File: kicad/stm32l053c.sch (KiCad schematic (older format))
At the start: 17 parts, among them P1 SWD, U1 STM32L053C8_LQFP48, U2 TLV61225, Y1 Crystal

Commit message: Buttons
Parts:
- added SW1, SW2, SW3: SW_PUSH, symbol SW_PUSH
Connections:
- net BUTTON0: now also SW1.2
- net BUTTON1: now also SW2.2
- net BUTTON2: now also SW3.2
- net VDD: now also SW1.1, SW2.1, SW3.1
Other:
- moved on the sheet: P1
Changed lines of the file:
@@
 $EndDescr
 $Comp
-L Earth #PWR4
+L Earth #PWR21
 U 1 1 58021BE1
 P 4900 7200
-F 0 "#PWR4" H 4900 6950 50  0001 C CNN
+F 0 "#PWR21" H 4900 6950 50  0001 C CNN
 F 1 "Earth" H 4900 7050 50  0001 C CNN
 F 2 "" H 4900 7200 50  0000 C CNN
@@
 $EndComp
 $Comp
-L VDD #PWR2
+L VDD #PWR19
 U 1 1 58021C2A
 P 4900 6900
-F 0 "#PWR2" H 4900 6750 50  0001 C CNN
+F 0 "#PWR19" H 4900 6750 50  0001 C CNN
 F 1 "VDD" H 4900 7050 50  0000 C CNN
 F 2 "" H 4900 6900 50  0000 C CNN
@@
 $EndComp
 $Comp
-L GNDA #PWR20
+L GNDA #PWR13
 U 1 1 58021F75
 P 5100 6300
-F 0 "#PWR20" H 5100 6050 50  0001 C CNN
+F 0 "#PWR13" H 5100 6050 50  0001 C CNN
 F 1 "GNDA" H 5100 6150 50  0000 C CNN
 F 2 "" H 5100 6300 50  0000 C CNN
@@
 $EndComp
 $Comp
-L Earth #PWR21
+L Earth #PWR14
 U 1 1 58021F89
 P 5600 6300
-F 0 "#PWR21" H 5600 6050 50  0001 C CNN
+F 0 "#PWR14" H 5600 6050 50  0001 C CNN
 F 1 "Earth" H 5600 6150 50  0001 C CNN
 F 2 "" H 5600 6300 50  0000 C CNN
@@
 $EndComp
 $Comp
-L GNDA #PWR18
+L GNDA #PWR11
 U 1 1 58022154
 P 5150 5800
-F 0 "#PWR18" H 5150 5550 50  0001 C CNN
+F 0 "#PWR11" H 5150 5550 50  0001 C CNN
 F 1 "GNDA" H 5150 5650 50  0000 C CNN
 F 2 "" H 5150 5800 50  0000 C CNN
@@
 $EndComp
 $Comp
-L Earth #PWR19
+L Earth #PWR12
 U 1 1 580221FA
 P 5650 5800
-F 0 "#PWR19" H 5650 5550 50  0001 C CNN
+F 0 "#PWR12" H 5650 5550 50  0001 C CNN
 F 1 "Earth" H 5650 5650 50  0001 C CNN
 F 2 "" H 5650 5800 50  0000 C CNN
@@
 $EndComp
 $Comp
-L Earth #PWR7
+L Earth #PWR4
 U 1 1 5803310F
 P 4800 1800
-F 0 "#PWR7" H 4800 1550 50  0001 C CNN
+F 0 "#PWR4" H 4800 1550 50  0001 C CNN
 F 1 "Earth" H 4800 1650 50  0001 C CNN
 F 2 "" H 4800 1800 50  0000 C CNN
@@
 L CONN_01X05 P1
 U 1 1 58036840
-P 1700 3550
-F 0 "P1" H 1700 3900 50  0000 C CNN
-F 1 "SWD" V 1800 3550 50  0000 C CNN
-F 2 "Pin_Headers:Pin_Header_Straight_1x06" H 1700 3550 50  0001 C CNN
-F 3 "" H 1700 3550 50  0000 C CNN
-	1    1700 3550
+P 1450 1400
+F 0 "P1" H 1450 1750 50  0000 C CNN
+F 1 "SWD" V 1550 1400 50  0000 C CNN
+F 2 "Pin_Headers:Pin_Header_Straight_1x06" H 1450 1400 50  0001 C CNN
+F 3 "" H 1450 1400 50  0000 C CNN
+	1    1450 1400
 	-1   0    0    -1
 $EndComp
 $Comp
-L Earth #PWR6
+L Earth #PWR3
 U 1 1 580369A9
-P 2400 3550
-F 0 "#PWR6" H 2400 3300 50  0001 C CNN
-F 1 "Earth" H 2400 3400 50  0001 C CNN
-F 2 "" H 2400 3550 50  0000 C CNN
-F 3 "" H 2400 3550 50  0000 C CNN
-	1    2400 3550
-	1    0    0    -1
-$EndComp
-Text GLabel 1900 3450 2    60   Input ~ 0
+P 2150 1400
+F 0 "#PWR3" H 2150 1150 50  0001 C CNN
+F 1 "Earth" H 2150 1250 50  0001 C CNN
+F 2 "" H 2150 1400 50  0000 C CNN
+F 3 "" H 2150 1400 50  0000 C CNN
+	1    2150 1400
+	1    0    0    -1
+$EndComp
+Text GLabel 1650 1300 2    60   Input ~ 0
 SWCLK
-Text GLabel 1900 3650 2    60   Input ~ 0
+Text GLabel 1650 1500 2    60   Input ~ 0
 SWDIO
-Text GLabel 1900 3750 2    60   Input ~ 0
+Text GLabel 1650 1600 2    60   Input ~ 0
 NRST
 $Comp
-L VDD #PWR3
+L VDD #PWR2
 U 1 1 5803734F
-P 1900 3350
-F 0 "#PWR3" H 1900 3200 50  0001 C CNN
-F 1 "VDD" H 1900 3500 50  0000 C CNN
-F 2 "" H 1900 3350 50  0000 C CNN
-F 3 "" H 1900 3350 50  0000 C CNN
-	1    1900 3350
+P 1650 1200
+F 0 "#PWR2" H 1650 1050 50  0001 C CNN
+F 1 "VDD" H 1650 1350 50  0000 C CNN
+F 2 "" H 1650 1200 50  0000 C CNN
+F 3 "" H 1650 1200 50  0000 C CNN
+	1    1650 1200
 	1    0    0    -1
 $EndComp
@@
 $EndComp
 $Comp
-L Earth #PWR5
+L Earth #PWR22
 U 1 1 5803BDC8
 P 5950 7200
-F 0 "#PWR5" H 5950 6950 50  0001 C CNN
+F 0 "#PWR22" H 5950 6950 50  0001 C CNN
 F 1 "Earth" H 5950 7050 50  0001 C CNN
 F 2 "" H 5950 7200 50  0000 C CNN
@@
 $EndComp
 $Comp
-L Earth #PWR16
+L Earth #PWR9
 U 1 1 58065816
 P 6550 5400
-F 0 "#PWR16" H 6550 5150 50  0001 C CNN
+F 0 "#PWR9" H 6550 5150 50  0001 C CNN
 F 1 "Earth" H 6550 5250 50  0001 C CNN
 F 2 "" H 6550 5400 50  0000 C CNN
@@
 	4050 3700 4600 3700
 Wire Wire Line
-	2400 3550 1900 3550
+	2150 1400 1650 1400
 Wire Wire Line
 	5600 6300 5100 6300
@@
 $EndComp
 $Comp
-L Earth #PWR17
+L Earth #PWR10
 U 1 1 5806680D
 P 3600 5700
-F 0 "#PWR17" H 3600 5450 50  0001 C CNN
+F 0 "#PWR10" H 3600 5450 50  0001 C CNN
 F 1 "Earth" H 3600 5550 50  0001 C CNN
 F 2 "" H 3600 5700 50  0000 C CNN
@@
 $EndComp
 $Comp
-L Earth #PWR15
+L Earth #PWR5
 U 1 1 58077163
 P 9600 2300
-F 0 "#PWR15" H 9600 2050 50  0001 C CNN
+F 0 "#PWR5" H 9600 2050 50  0001 C CNN
 F 1 "Earth" H 9600 2150 50  0001 C CNN
 F 2 "" H 9600 2300 50  0000 C CNN
@@
 $EndComp
 $Comp
-L +BATT #PWR10
+L +BATT #PWR16
 U 1 1 584F2368
 P 850 6750
-F 0 "#PWR10" H 850 6600 50  0001 C CNN
+F 0 "#PWR16" H 850 6600 50  0001 C CNN
 F 1 "+BATT" H 850 6890 50  0000 C CNN
 F 2 "" H 850 6750 50  0000 C CNN
@@
 Connection ~ 2700 6550
 $Comp
-L Earth #PWR13
+L Earth #PWR18
 U 1 1 584F287E
 P 2850 6850
-F 0 "#PWR13" H 2850 6600 50  0001 C CNN
+F 0 "#PWR18" H 2850 6600 50  0001 C CNN
 F 1 "Earth" H 2850 6700 50  0001 C CNN
 F 2 "" H 2850 6850 50  0000 C CNN
@@
 $EndComp
 $Comp
-L Earth #PWR12
+L Earth #PWR17
 U 1 1 584F28E3
 P 1700 6850
-F 0 "#PWR12" H 1700 6600 50  0001 C CNN
+F 0 "#PWR17" H 1700 6600 50  0001 C CNN
 F 1 "Earth" H 1700 6700 50  0001 C CNN
 F 2 "" H 1700 6850 50  0000 C CNN
@@
 $EndComp
 $Comp
-L Earth #PWR14
+L Earth #PWR20
 U 1 1 584F2924
 P 1250 7050
-F 0 "#PWR14" H 1250 6800 50  0001 C CNN
+F 0 "#PWR20" H 1250 6800 50  0001 C CNN
 F 1 "Earth" H 1250 6900 50  0001 C CNN
 F 2 "" H 1250 7050 50  0000 C CNN
@@
 $EndComp
 $Comp
-L VDD #PWR9
+L VDD #PWR15
 U 1 1 584F2A51
 P 3200 6550
-F 0 "#PWR9" H 3200 6400 50  0001 C CNN
+F 0 "#PWR15" H 3200 6400 50  0001 C CNN
 F 1 "VDD" H 3200 6700 50  0000 C CNN
 F 2 "" H 3200 6550 50  0000 C CNN
@@
 Wire Wire Line
 	8500 4550 9050 4550
+$Comp
+L SW_PUSH SW1
+U 1 1 5850680E
+P 1700 2900
+F 0 "SW1" H 1850 3010 50  0000 C CNN
+F 1 "SW_PUSH" H 1700 2820 50  0000 C CNN
+F 2 "" H 1700 2900 50  0000 C CNN
+F 3 "" H 1700 2900 50  0000 C CNN
+	1    1700 2900
+	1    0    0    -1
+$EndComp
+$Comp
+L VDD #PWR6
+U 1 1 585069C3
+P 1300 2750
+F 0 "#PWR6" H 1300 2600 50  0001 C CNN
+F 1 "VDD" H 1300 2900 50  0000 C CNN
+F 2 "" H 1300 2750 50  0000 C CNN
+F 3 "" H 1300 2750 50  0000 C CNN
+	1    1300 2750
+	1    0    0    -1
+$EndComp
+Text Label 2550 2900 2    60   ~ 0
+BUTTON0
+Wire Wire Line
+	1300 2750 1300 2900
+Wire Wire Line
+	1300 2900 1400 2900
+Wire Wire Line
+	2000 2900 2550 2900
+$Comp
+L SW_PUSH SW2
+U 1 1 58506BDE
+P 1700 3450
+F 0 "SW2" H 1850 3560 50  0000 C CNN
+F 1 "SW_PUSH" H 1700 3370 50  0000 C CNN
+F 2 "" H 1700 3450 50  0000 C CNN
+F 3 "" H 1700 3450 50  0000 C CNN
+	1    1700 3450
+	1    0    0    -1
+$EndComp
+$Comp
+L VDD #PWR7
+U 1 1 58506BE4
+P 1300 3300
+F 0 "#PWR7" H 1300 3150 50  0001 C CNN
+F 1 "VDD" H 1300 3450 50  0000 C CNN
+F 2 "" H 1300 3300 50  0000 C CNN
+F 3 "" H 1300 3300 50  0000 C CNN
+	1    1300 3300
+	1    0    0    -1
+$EndComp
+Text Label 2550 3450 2    60   ~ 0
+BUTTON1
+Wire Wire Line
+	1300 3300 1300 3450
+Wire Wire Line
+	1300 3450 1400 3450
+Wire Wire Line
+	2000 3450 2550 3450
+$Comp
+L SW_PUSH SW3
+U 1 1 58506C80
+P 1700 4050
+F 0 "SW3" H 1850 4160 50  0000 C CNN
+F 1 "SW_PUSH" H 1700 3970 50  0000 C CNN
+F 2 "" H 1700 4050 50  0000 C CNN
+F 3 "" H 1700 4050 50  0000 C CNN
+	1    1700 4050
+	1    0    0    -1
+$EndComp
+$Comp
+L VDD #PWR8
+U 1 1 58506C86
+P 1300 3900
+F 0 "#PWR8" H 1300 3750 50  0001 C CNN
+F 1 "VDD" H 1300 4050 50  0000 C CNN
+F 2 "" H 1300 3900 50  0000 C CNN
+F 3 "" H 1300 3900 50  0000 C CNN
+	1    1300 3900
+	1    0    0    -1
+$EndComp
+Text Label 2550 4050 2    60   ~ 0
+BUTTON2
+Wire Wire Line
+	1300 3900 1300 4050
+Wire Wire Line
+	1300 4050 1400 4050
+Wire Wire Line
+	2000 4050 2550 4050
 $EndSCHEMATC

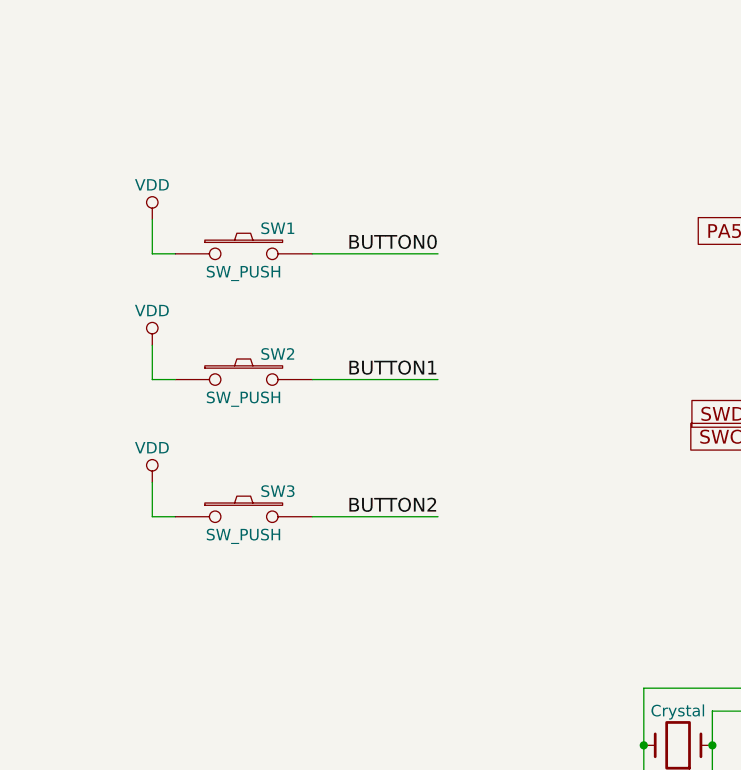
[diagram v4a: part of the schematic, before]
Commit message: Button debounce
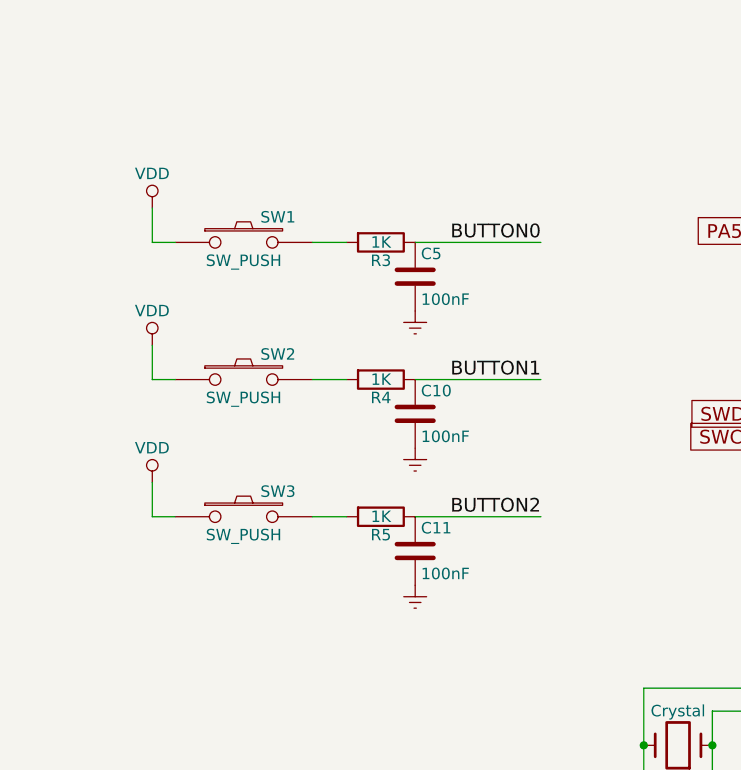
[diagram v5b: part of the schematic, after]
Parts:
- added C10, C11, C5: 100nF, symbol C
- added R3, R4, R5: 1K, symbol R
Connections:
- net BUTTON0: now also C5.1, R3.1; no longer SW1.2
- net BUTTON1: now also C10.1, R4.1; no longer SW2.2
- net BUTTON2: now also C11.1, R5.1; no longer SW3.2
- net Earth: now also C10.2, C11.2, C5.2
- new net: R3.2, SW1.2
- new net: R4.2, SW2.2
- new net: R5.2, SW3.2
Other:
- moved on the sheet: SW1
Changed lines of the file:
@@
 $EndDescr
 $Comp
-L Earth #PWR21
+L Earth #PWR24
 U 1 1 58021BE1
 P 4900 7200
-F 0 "#PWR21" H 4900 6950 50  0001 C CNN
+F 0 "#PWR24" H 4900 6950 50  0001 C CNN
 F 1 "Earth" H 4900 7050 50  0001 C CNN
 F 2 "" H 4900 7200 50  0000 C CNN
@@
 $EndComp
 $Comp
-L VDD #PWR19
+L VDD #PWR22
 U 1 1 58021C2A
 P 4900 6900
-F 0 "#PWR19" H 4900 6750 50  0001 C CNN
+F 0 "#PWR22" H 4900 6750 50  0001 C CNN
 F 1 "VDD" H 4900 7050 50  0000 C CNN
 F 2 "" H 4900 6900 50  0000 C CNN
@@
 $EndComp
 $Comp
-L GNDA #PWR13
+L GNDA #PWR16
 U 1 1 58021F75
 P 5100 6300
-F 0 "#PWR13" H 5100 6050 50  0001 C CNN
+F 0 "#PWR16" H 5100 6050 50  0001 C CNN
 F 1 "GNDA" H 5100 6150 50  0000 C CNN
 F 2 "" H 5100 6300 50  0000 C CNN
@@
 $EndComp
 $Comp
-L Earth #PWR14
+L Earth #PWR17
 U 1 1 58021F89
 P 5600 6300
-F 0 "#PWR14" H 5600 6050 50  0001 C CNN
+F 0 "#PWR17" H 5600 6050 50  0001 C CNN
 F 1 "Earth" H 5600 6150 50  0001 C CNN
 F 2 "" H 5600 6300 50  0000 C CNN
@@
 $EndComp
 $Comp
-L GNDA #PWR11
+L GNDA #PWR14
 U 1 1 58022154
 P 5150 5800
-F 0 "#PWR11" H 5150 5550 50  0001 C CNN
+F 0 "#PWR14" H 5150 5550 50  0001 C CNN
 F 1 "GNDA" H 5150 5650 50  0000 C CNN
 F 2 "" H 5150 5800 50  0000 C CNN
@@
 $EndComp
 $Comp
-L Earth #PWR12
+L Earth #PWR15
 U 1 1 580221FA
 P 5650 5800
-F 0 "#PWR12" H 5650 5550 50  0001 C CNN
+F 0 "#PWR15" H 5650 5550 50  0001 C CNN
 F 1 "Earth" H 5650 5650 50  0001 C CNN
 F 2 "" H 5650 5800 50  0000 C CNN
@@
 $EndComp
 $Comp
-L Earth #PWR22
+L Earth #PWR25
 U 1 1 5803BDC8
 P 5950 7200
-F 0 "#PWR22" H 5950 6950 50  0001 C CNN
+F 0 "#PWR25" H 5950 6950 50  0001 C CNN
 F 1 "Earth" H 5950 7050 50  0001 C CNN
 F 2 "" H 5950 7200 50  0000 C CNN
@@
 $EndComp
 $Comp
-L Earth #PWR9
+L Earth #PWR12
 U 1 1 58065816
 P 6550 5400
-F 0 "#PWR9" H 6550 5150 50  0001 C CNN
+F 0 "#PWR12" H 6550 5150 50  0001 C CNN
 F 1 "Earth" H 6550 5250 50  0001 C CNN
 F 2 "" H 6550 5400 50  0000 C CNN
@@
 $EndComp
 $Comp
-L Earth #PWR10
+L Earth #PWR13
 U 1 1 5806680D
 P 3600 5700
-F 0 "#PWR10" H 3600 5450 50  0001 C CNN
+F 0 "#PWR13" H 3600 5450 50  0001 C CNN
 F 1 "Earth" H 3600 5550 50  0001 C CNN
 F 2 "" H 3600 5700 50  0000 C CNN
@@
 $EndComp
 $Comp
-L +BATT #PWR16
+L +BATT #PWR19
 U 1 1 584F2368
 P 850 6750
-F 0 "#PWR16" H 850 6600 50  0001 C CNN
+F 0 "#PWR19" H 850 6600 50  0001 C CNN
 F 1 "+BATT" H 850 6890 50  0000 C CNN
 F 2 "" H 850 6750 50  0000 C CNN
@@
 Connection ~ 2700 6550
 $Comp
-L Earth #PWR18
+L Earth #PWR21
 U 1 1 584F287E
 P 2850 6850
-F 0 "#PWR18" H 2850 6600 50  0001 C CNN
+F 0 "#PWR21" H 2850 6600 50  0001 C CNN
 F 1 "Earth" H 2850 6700 50  0001 C CNN
 F 2 "" H 2850 6850 50  0000 C CNN
@@
 $EndComp
 $Comp
-L Earth #PWR17
+L Earth #PWR20
 U 1 1 584F28E3
 P 1700 6850
-F 0 "#PWR17" H 1700 6600 50  0001 C CNN
+F 0 "#PWR20" H 1700 6600 50  0001 C CNN
 F 1 "Earth" H 1700 6700 50  0001 C CNN
 F 2 "" H 1700 6850 50  0000 C CNN
@@
 $EndComp
 $Comp
-L Earth #PWR20
+L Earth #PWR23
 U 1 1 584F2924
 P 1250 7050
-F 0 "#PWR20" H 1250 6800 50  0001 C CNN
+F 0 "#PWR23" H 1250 6800 50  0001 C CNN
 F 1 "Earth" H 1250 6900 50  0001 C CNN
 F 2 "" H 1250 7050 50  0000 C CNN
@@
 $EndComp
 $Comp
-L VDD #PWR15
+L VDD #PWR18
 U 1 1 584F2A51
 P 3200 6550
-F 0 "#PWR15" H 3200 6400 50  0001 C CNN
+F 0 "#PWR18" H 3200 6400 50  0001 C CNN
 F 1 "VDD" H 3200 6700 50  0000 C CNN
 F 2 "" H 3200 6550 50  0000 C CNN
@@
 L SW_PUSH SW1
 U 1 1 5850680E
-P 1700 2900
-F 0 "SW1" H 1850 3010 50  0000 C CNN
-F 1 "SW_PUSH" H 1700 2820 50  0000 C CNN
-F 2 "" H 1700 2900 50  0000 C CNN
-F 3 "" H 1700 2900 50  0000 C CNN
-	1    1700 2900
+P 1700 2850
+F 0 "SW1" H 1850 2960 50  0000 C CNN
+F 1 "SW_PUSH" H 1700 2770 50  0000 C CNN
+F 2 "" H 1700 2850 50  0000 C CNN
+F 3 "" H 1700 2850 50  0000 C CNN
+	1    1700 2850
 	1    0    0    -1
 $EndComp
@@
 L VDD #PWR6
 U 1 1 585069C3
-P 1300 2750
-F 0 "#PWR6" H 1300 2600 50  0001 C CNN
-F 1 "VDD" H 1300 2900 50  0000 C CNN
-F 2 "" H 1300 2750 50  0000 C CNN
-F 3 "" H 1300 2750 50  0000 C CNN
-	1    1300 2750
-	1    0    0    -1
-$EndComp
-Text Label 2550 2900 2    60   ~ 0
+P 1300 2700
+F 0 "#PWR6" H 1300 2550 50  0001 C CNN
+F 1 "VDD" H 1300 2850 50  0000 C CNN
+F 2 "" H 1300 2700 50  0000 C CNN
+F 3 "" H 1300 2700 50  0000 C CNN
+	1    1300 2700
+	1    0    0    -1
+$EndComp
+Text Label 3000 2850 2    60   ~ 0
 BUTTON0
 Wire Wire Line
-	1300 2750 1300 2900
-Wire Wire Line
-	1300 2900 1400 2900
-Wire Wire Line
-	2000 2900 2550 2900
+	1300 2700 1300 2850
+Wire Wire Line
+	1300 2850 1400 2850
 $Comp
 L SW_PUSH SW2
@@
 $EndComp
 $Comp
-L VDD #PWR7
+L VDD #PWR8
 U 1 1 58506BE4
 P 1300 3300
-F 0 "#PWR7" H 1300 3150 50  0001 C CNN
+F 0 "#PWR8" H 1300 3150 50  0001 C CNN
 F 1 "VDD" H 1300 3450 50  0000 C CNN
 F 2 "" H 1300 3300 50  0000 C CNN
@@
 	1    0    0    -1
 $EndComp
-Text Label 2550 3450 2    60   ~ 0
+Text Label 3000 3450 2    60   ~ 0
 BUTTON1
 Wire Wire Line
@@
 Wire Wire Line
 	1300 3450 1400 3450
-Wire Wire Line
-	2000 3450 2550 3450
 $Comp
 L SW_PUSH SW3
@@
 $EndComp
 $Comp
-L VDD #PWR8
+L VDD #PWR10
 U 1 1 58506C86
 P 1300 3900
-F 0 "#PWR8" H 1300 3750 50  0001 C CNN
+F 0 "#PWR10" H 1300 3750 50  0001 C CNN
 F 1 "VDD" H 1300 4050 50  0000 C CNN
 F 2 "" H 1300 3900 50  0000 C CNN
@@
 	1    0    0    -1
 $EndComp
-Text Label 2550 4050 2    60   ~ 0
+Text Label 3000 4050 2    60   ~ 0
 BUTTON2
 Wire Wire Line
@@
 Wire Wire Line
 	1300 4050 1400 4050
-Wire Wire Line
-	2000 4050 2550 4050
+$Comp
+L R R3
+U 1 1 58519B61
+P 2300 2850
+F 0 "R3" V 2380 2850 50  0000 C CNN
+F 1 "1K" V 2300 2850 50  0000 C CNN
+F 2 "" V 2230 2850 50  0000 C CNN
+F 3 "" H 2300 2850 50  0000 C CNN
+	1    2300 2850
+	0    1    1    0
+$EndComp
+$Comp
+L R R4
+U 1 1 58519D14
+P 2300 3450
+F 0 "R4" V 2380 3450 50  0000 C CNN
+F 1 "1K" V 2300 3450 50  0000 C CNN
+F 2 "" V 2230 3450 50  0000 C CNN
+F 3 "" H 2300 3450 50  0000 C CNN
+	1    2300 3450
+	0    1    1    0
+$EndComp
+$Comp
+L R R5
+U 1 1 58519D86
+P 2300 4050
+F 0 "R5" V 2380 4050 50  0000 C CNN
+F 1 "1K" V 2300 4050 50  0000 C CNN
+F 2 "" V 2230 4050 50  0000 C CNN
+F 3 "" H 2300 4050 50  0000 C CNN
+	1    2300 4050
+	0    1    1    0
+$EndComp
+Wire Wire Line
+	2150 2850 2000 2850
+Wire Wire Line
+	2000 3450 2150 3450
+Wire Wire Line
+	2000 4050 2150 4050
+Wire Wire Line
+	2450 3450 3000 3450
+Wire Wire Line
+	2450 4050 3000 4050
+$Comp
+L C C5
+U 1 1 5851A24C
+P 2450 3000
+F 0 "C5" H 2475 3100 50  0000 L CNN
+F 1 "100nF" H 2475 2900 50  0000 L CNN
+F 2 "" H 2488 2850 50  0000 C CNN
+F 3 "" H 2450 3000 50  0000 C CNN
+	1    2450 3000
+	1    0    0    -1
+$EndComp
+Wire Wire Line
+	2450 2850 3000 2850
+$Comp
+L Earth #PWR7
+U 1 1 5851A35F
+P 2450 3150
+F 0 "#PWR7" H 2450 2900 50  0001 C CNN
+F 1 "Earth" H 2450 3000 50  0001 C CNN
+F 2 "" H 2450 3150 50  0000 C CNN
+F 3 "" H 2450 3150 50  0000 C CNN
+	1    2450 3150
+	1    0    0    -1
+$EndComp
+$Comp
+L C C10
+U 1 1 5851A3FF
+P 2450 3600
+F 0 "C10" H 2475 3700 50  0000 L CNN
+F 1 "100nF" H 2475 3500 50  0000 L CNN
+F 2 "" H 2488 3450 50  0000 C CNN
+F 3 "" H 2450 3600 50  0000 C CNN
+	1    2450 3600
+	1    0    0    -1
+$EndComp
+$Comp
+L C C11
+U 1 1 5851A470
+P 2450 4200
+F 0 "C11" H 2475 4300 50  0000 L CNN
+F 1 "100nF" H 2475 4100 50  0000 L CNN
+F 2 "" H 2488 4050 50  0000 C CNN
+F 3 "" H 2450 4200 50  0000 C CNN
+	1    2450 4200
+	1    0    0    -1
+$EndComp
+$Comp
+L Earth #PWR9
+U 1 1 5851A4F4
+P 2450 3750
+F 0 "#PWR9" H 2450 3500 50  0001 C CNN
+F 1 "Earth" H 2450 3600 50  0001 C CNN
+F 2 "" H 2450 3750 50  0000 C CNN
+F 3 "" H 2450 3750 50  0000 C CNN
+	1    2450 3750
+	1    0    0    -1
+$EndComp
+$Comp
+L Earth #PWR11
+U 1 1 5851A54D
+P 2450 4350
+F 0 "#PWR11" H 2450 4100 50  0001 C CNN
+F 1 "Earth" H 2450 4200 50  0001 C CNN
+F 2 "" H 2450 4350 50  0000 C CNN
+F 3 "" H 2450 4350 50  0000 C CNN
+	1    2450 4350
+	1    0    0    -1
+$EndComp
 $EndSCHEMATC

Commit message: Buzzer
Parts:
- added LS?: BUZZER, symbol BUZZER
- added Q?: Q_NPN_CBE, symbol Q_NPN_CBE
- added R?: 1K, symbol R
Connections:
- net Earth: now also Q?.3 (E)
- net VDD: now also LS?.1 (+)
- new net: LS?.2 (-), Q?.1 (C)
- new net: Q?.2 (B), R?.1
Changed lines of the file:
@@
+	1    0    0    -1
+$EndComp
+$Comp
+L BUZZER LS?
+U 1 1 5851ABB3
+P 9500 5200
+F 0 "LS?" H 9500 5450 60  0000 C CNN
+F 1 "BUZZER" H 9500 4950 60  0000 C CNN
+F 2 "" H 9650 5450 60  0001 C CNN
+F 3 "" H 9650 5450 60  0001 C CNN
+	1    9500 5200
+	1    0    0    -1
+$EndComp
+$Comp
+L Q_NPN_CBE Q?
+U 1 1 5851AC3A
+P 9200 5650
+F 0 "Q?" H 9500 5700 50  0000 R CNN
+F 1 "Q_NPN_CBE" H 9800 5600 50  0000 R CNN
+F 2 "" H 9400 5750 50  0000 C CNN
+F 3 "" H 9200 5650 50  0000 C CNN
+	1    9200 5650
+	1    0    0    -1
+$EndComp
+$Comp
+L R R?
+U 1 1 5851ADE5
+P 8750 5650
+F 0 "R?" V 8830 5650 50  0000 C CNN
+F 1 "1K" V 8750 5650 50  0000 C CNN
+F 2 "" V 8680 5650 50  0000 C CNN
+F 3 "" H 8750 5650 50  0000 C CNN
+	1    8750 5650
+	0    1    1    0
+$EndComp
+Wire Wire Line
+	9300 5250 9300 5450
+Wire Wire Line
+	9000 5650 8900 5650
+Wire Wire Line
+	8600 5650 8200 5650
+$Comp
+L Earth #PWR?
+U 1 1 5851B22D
+P 9300 5850
+F 0 "#PWR?" H 9300 5600 50  0001 C CNN
+F 1 "Earth" H 9300 5700 50  0001 C CNN
+F 2 "" H 9300 5850 50  0000 C CNN
+F 3 "" H 9300 5850 50  0000 C CNN
+	1    9300 5850
+	1    0    0    -1
+$EndComp
+$Comp
+L VDD #PWR?
+U 1 1 5851B377
+P 9300 5150
+F 0 "#PWR?" H 9300 5000 50  0001 C CNN
+F 1 "VDD" H 9300 5300 50  0000 C CNN
+F 2 "" H 9300 5150 50  0000 C CNN
+F 3 "" H 9300 5150 50  0000 C CNN
+	1    9300 5150
 	1    0    0    -1
 $EndComp
